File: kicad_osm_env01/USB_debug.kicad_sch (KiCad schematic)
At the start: 36 parts, among them J3 USB_B_Micro, Q2 S8050, Q3 S8050, U13 CP2102N-A01-GQFN24, U15 M74VHC1GT14DFT2G, U5 SP3003-02JTG

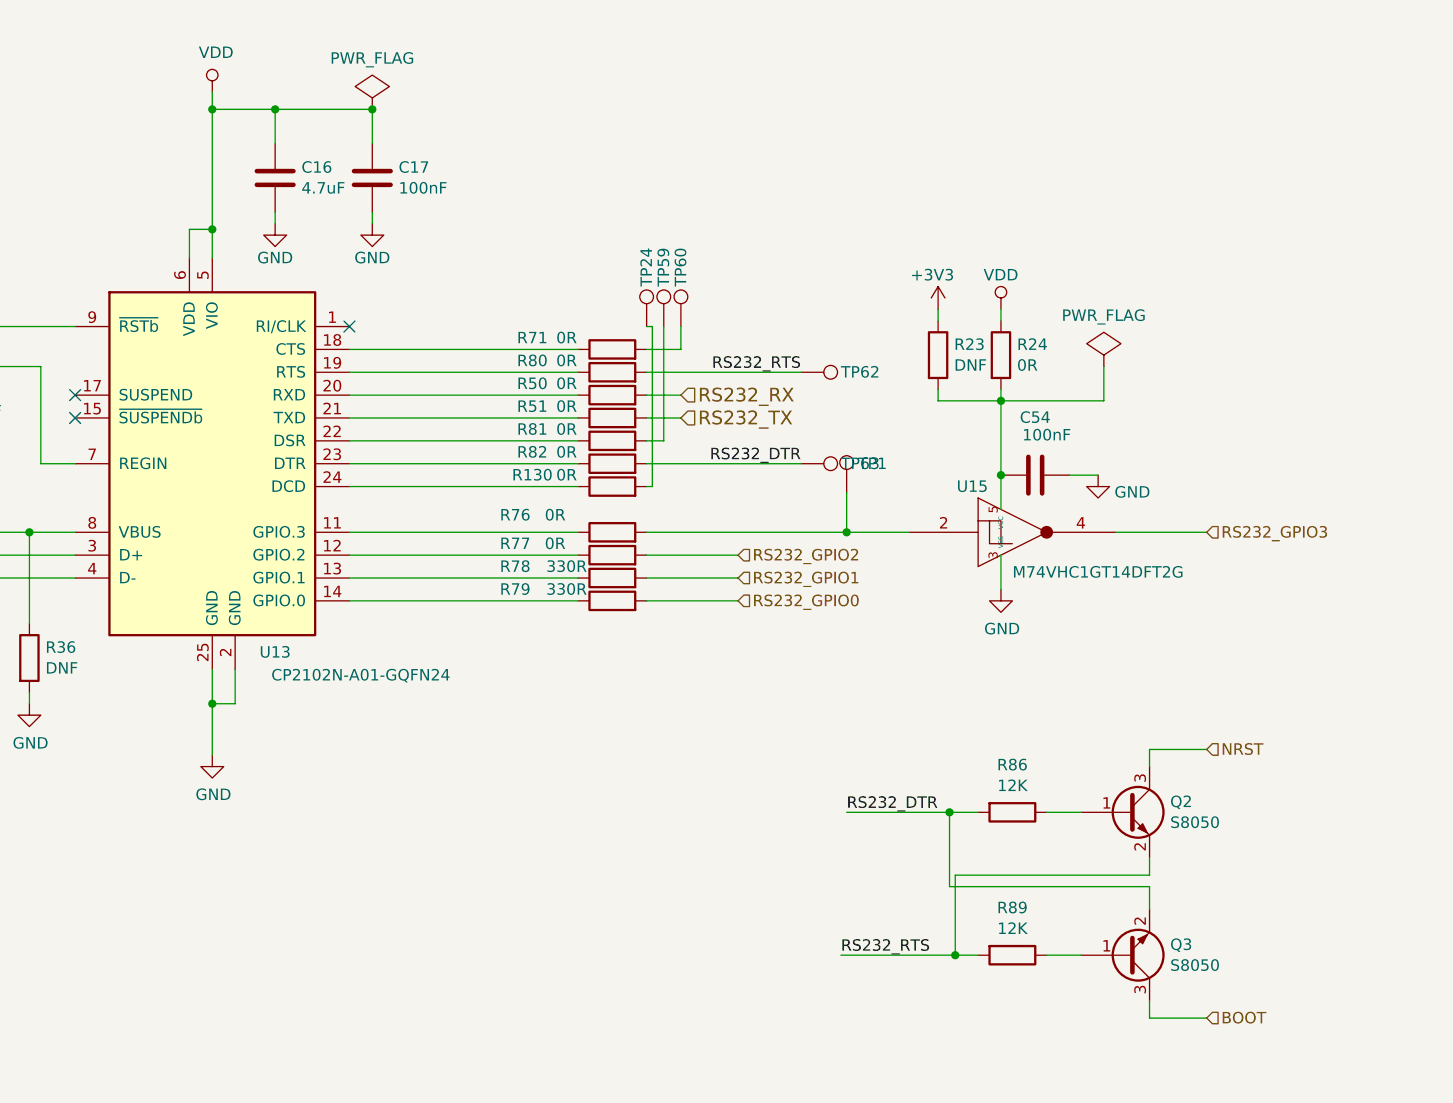
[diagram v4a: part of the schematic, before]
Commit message: Schematics waiting review
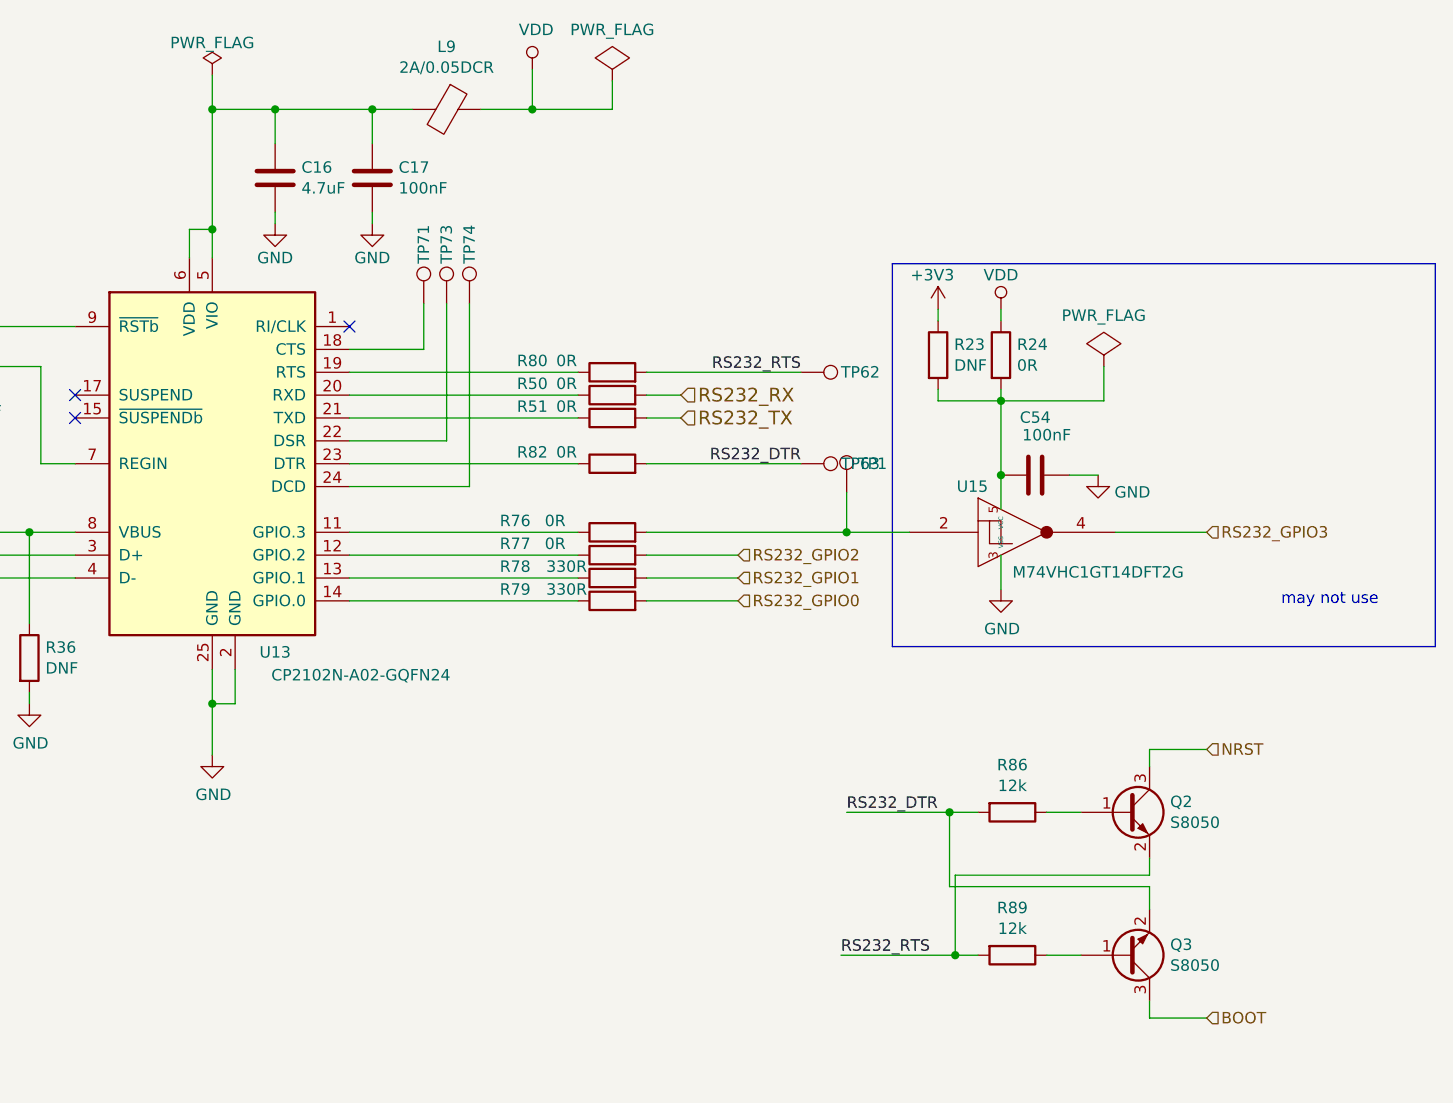
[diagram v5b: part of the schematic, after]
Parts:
- removed R130, R71, R81: 0R, Resistor_SMD:R_0603_1608Metric, symbol OSM_env01-rescue:R-device-ESP32-EVB_Rev_D-rescue
- removed TP24, TP59, TP60: Test_Point, TestPoint:TestPoint_Pad_D1.5mm, symbol Connector:Test_Point
- added L9: 2A/0.05DCR, Inductor_SMD:L_0402_1005Metric, symbol device:Ferrite_Bead
- added TP71, TP73, TP74: Test_Point, TestPoint:TestPoint_Pad_D1.5mm, symbol Connector:Test_Point
- R86, R89: value 12K -> 12k
- U13: value CP2102N-A01-GQFN24 -> CP2102N-A02-GQFN24
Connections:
- net VDD: now also L9.1; no longer C16.1, C17.1, U13.5 (VIO), U13.6 (VDD)
- net at U13.18 (CTS): now also TP71.1
- net at U13.22 (DSR): now also TP73.1
- net at U13.24 (DCD): now also TP74.1
- new net: C16.1, C17.1, L9.2, U13.5 (VIO), U13.6 (VDD)
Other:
- note added: "may not use"

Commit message: before fixing devtank symbol issues
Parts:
- added R152, R153: 0R, Resistor_SMD:R_0603_1608Metric, symbol device:R
- J3: value USB_B_Micro -> (none); footprint Devtank_PCB_lib:MOLEX_105017-0001_USB_B -> (none)
- TP1, TP63, TP71, TP73, TP74: value Test_Point -> (none); footprint TestPoint:TestPoint_Pad_D1.5mm -> (none); symbol Connector:Test_Point -> Connector:TestPoint
- TP62: footprint TestPoint:TestPoint_Pad_D1.5mm -> (none); symbol Connector:Test_Point -> Connector:TestPoint
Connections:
- net BOOT: now also R153.2; no longer Q3.3 (C)
- net NRST: now also R152.2; no longer Q2.3 (C)
- new net: Q2.3 (C), R152.1
- new net: Q3.3 (C), R153.1
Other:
- moved on the sheet: C54, R23, R24, TP1, U15

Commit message: started layout with throwdown
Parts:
- added R49: (no value), symbol Device:R
- added TP78: (no value), symbol Connector:TestPoint
- C15, C17, C54: value 100nF -> (none); footprint Capacitor_SMD:C_0402_1005Metric -> (none); symbol OSM_env01-rescue:C-device-ESP32-EVB_Rev_D-rescue -> Device:C
- C16: value 4.7uF -> (none); footprint Capacitor_SMD:C_0603_1608Metric -> (none); symbol OSM_env01-rescue:C-device-ESP32-EVB_Rev_D-rescue -> Device:C
- C47: value 4.7uF -> (none); footprint Capacitor_SMD:C_0603_1608Metric -> (none); symbol device:C -> Device:C
- C48: value 100nF -> (none); footprint Capacitor_SMD:C_0402_1005Metric -> (none); symbol device:C -> Device:C
- L9: value 2A/0.05DCR -> (none); footprint Inductor_SMD:L_0402_1005Metric -> (none); symbol device:Ferrite_Bead -> Device:FerriteBead
- Q2, Q3: value S8050 -> (none); footprint Package_TO_SOT_SMD:SOT-23 -> (none); symbol device:Q_NPN_BEC -> Device:Q_NPN_BEC
- R152, R153, R24, R35: value 0R -> (none); footprint Resistor_SMD:R_0603_1608Metric -> (none); symbol device:R -> Device:R
- R23, R36: value DNF -> (none); footprint Resistor_SMD:R_0603_1608Metric -> (none); symbol device:R -> Device:R
- R48: value 10k -> (none); footprint Resistor_SMD:R_0603_1608Metric -> (none); symbol OSM_env01-rescue:R-device-ESP32-EVB_Rev_D-rescue -> Device:R
- R50, R51, R76, R77, R80, R82: value 0R -> (none); footprint Resistor_SMD:R_0603_1608Metric -> (none); symbol OSM_env01-rescue:R-device-ESP32-EVB_Rev_D-rescue -> Device:R
- R78, R79: value 330R -> (none); footprint Resistor_SMD:R_0603_1608Metric -> (none); symbol OSM_env01-rescue:R-device-ESP32-EVB_Rev_D-rescue -> Device:R
- R86, R89: value 12k -> (none); footprint Resistor_SMD:R_0603_1608Metric -> (none); symbol device:R -> Device:R
- TP62: value Test_Point -> (none)
- U13: value CP2102N-A02-GQFN24 -> (none); footprint Devtank_PCB_lib:CP2102_QFN-24-1EP_4x4mm_P0.5mm_EP2.6x2.6mm_ThermalVias_0.3mmdrill -> (none)
- U15: value M74VHC1GT14DFT2G -> (none); footprint Package_TO_SOT_SMD:SOT-353_SC-70-5 -> (none)
- U5: value SP3003-02JTG -> (none); footprint Package_TO_SOT_SMD:SOT-353_SC-70-5 -> (none)
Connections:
- net BOOT is gone; now on an unnamed net: R153.2
- net at TP1.1, U15.2: no longer R76.2
- net RS232_DTR renamed USB_DEBUG_DTR
- net RS232_GPIO0 renamed USB_DEBUG_GPIO0
- net RS232_GPIO1 renamed USB_DEBUG_GPIO1
- net RS232_GPIO2 renamed USB_DEBUG_GPIO2
- net RS232_GPIO3: no longer names the net of U15.4
- net RS232_GPIO3: now also R49.1, TP78.1
- net RS232_RTS renamed USB_DEBUG_RTS
- net RS232_RX renamed USB_DEBUG_RX
- net RS232_TX renamed USB_DEBUG_TX
- new net BOOT0: R49.2
- new net USB_DEBUG_GPIO3: R76.2
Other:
- note removed: "may not use"
- moved on the sheet: C54, Q2, Q3, R152, R153, R23, R24, R86, R89, U15

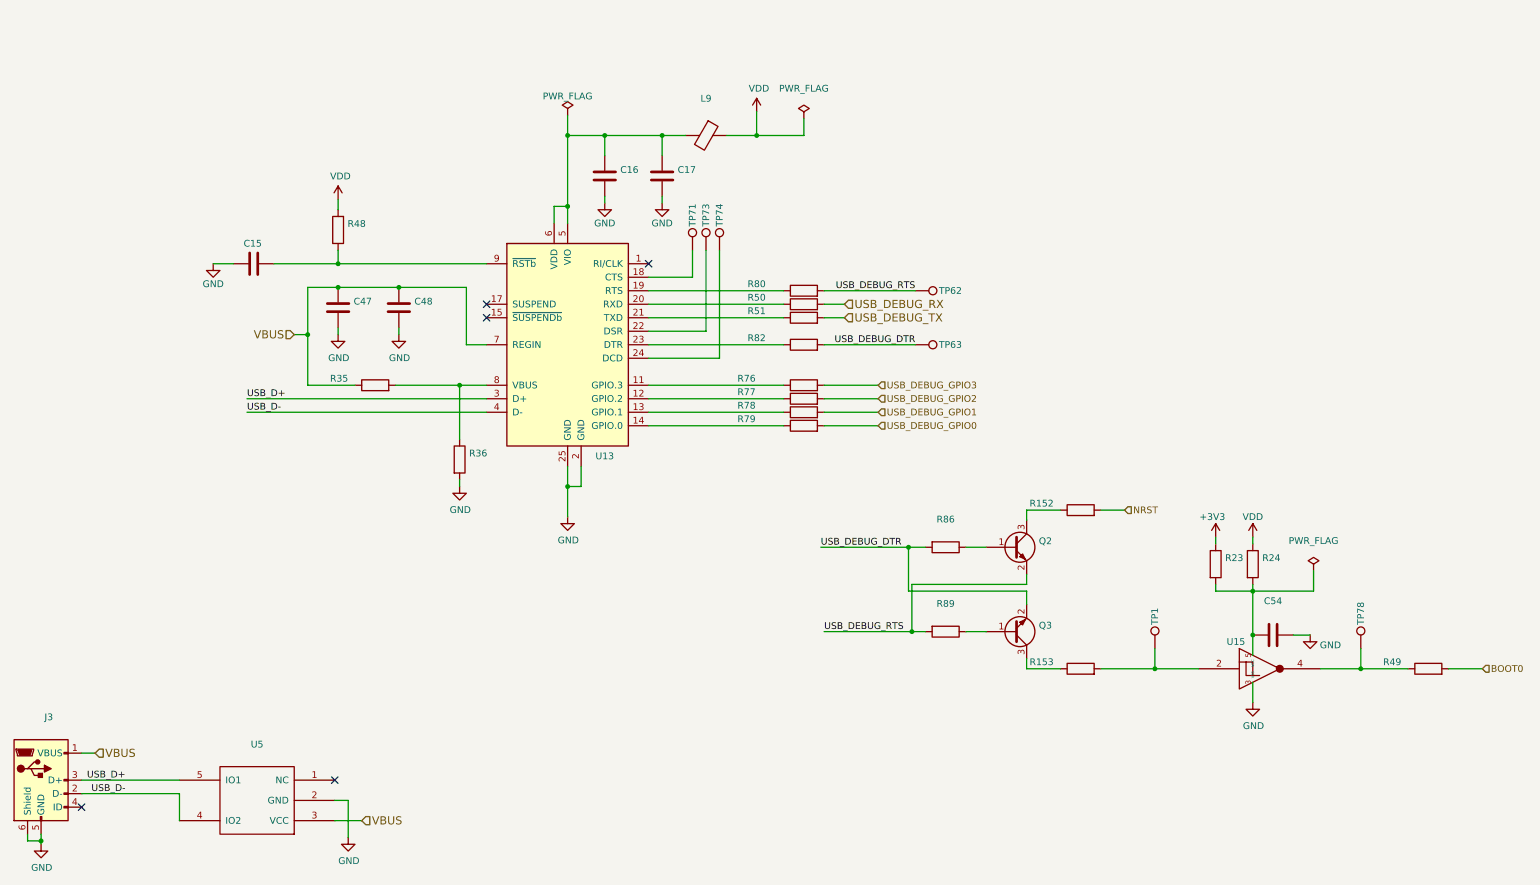
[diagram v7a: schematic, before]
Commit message: majority of signals routed on layout
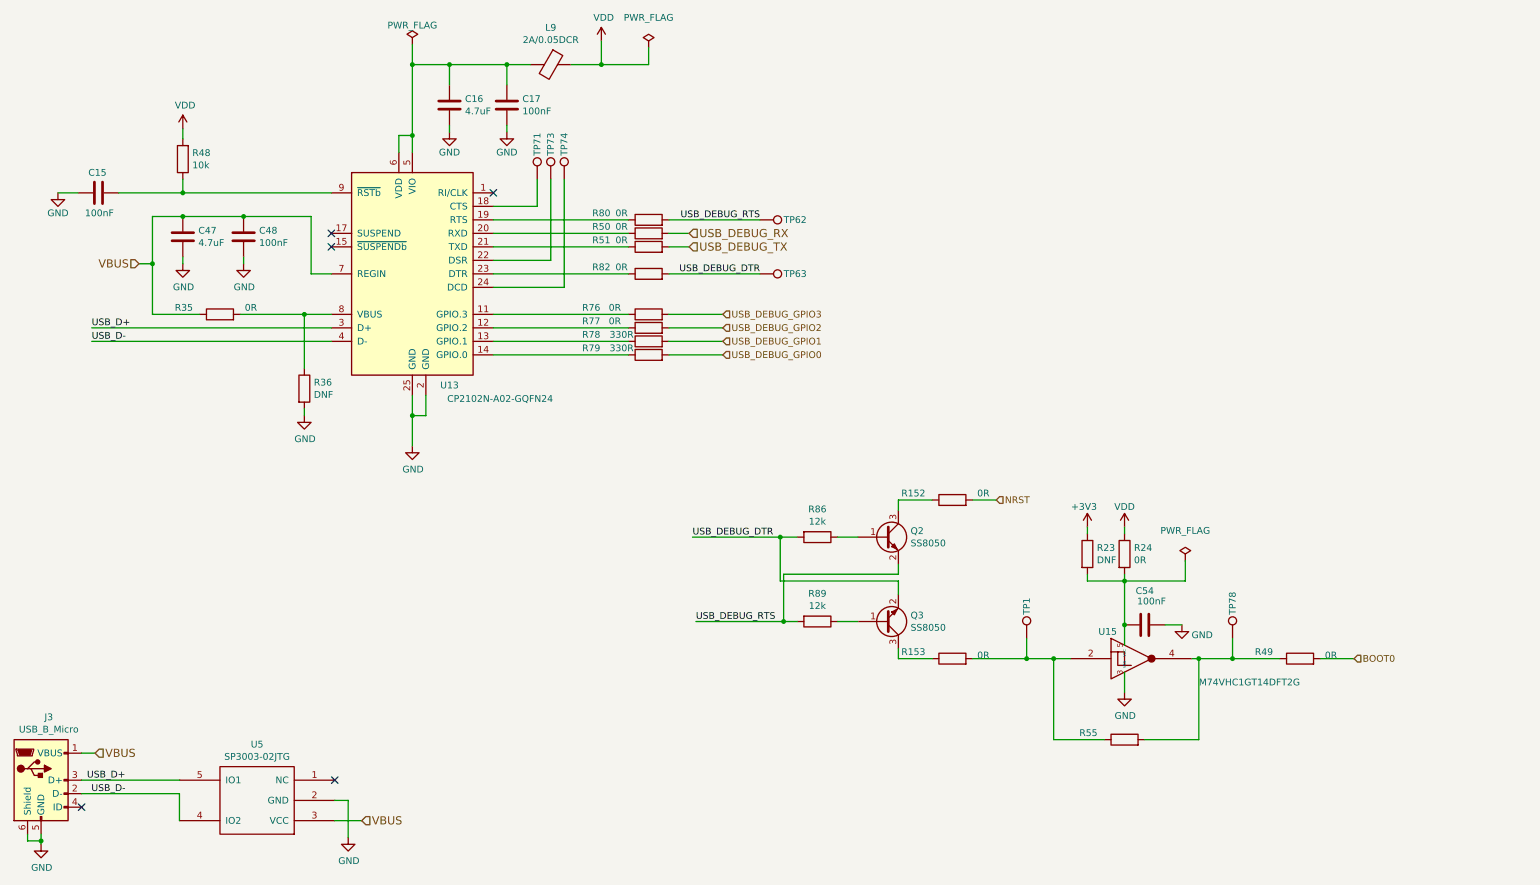
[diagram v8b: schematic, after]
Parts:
- added R55: (no value), symbol Device:R
- C15, C17, C48, C54: value (none) -> 100nF; footprint (none) -> Capacitor_SMD:C_0402_1005Metric
- C16, C47: value (none) -> 4.7uF; footprint (none) -> Capacitor_SMD:C_0402_1005Metric
- J3: value (none) -> USB_B_Micro; footprint (none) -> Devtank_PCB_lib:MOLEX_105017-0001_USB_B
- L9: value (none) -> 2A/0.05DCR; footprint (none) -> Inductor_SMD:L_0402_1005Metric
- Q2, Q3: value (none) -> SS8050; footprint (none) -> Package_TO_SOT_SMD:SOT-23
- R152, R153, R24, R35, R49, R50, R51, R76, R77, R80, R82: value (none) -> 0R; footprint (none) -> Resistor_SMD:R_0603_1608Metric
- R23, R36: value (none) -> DNF; footprint (none) -> Resistor_SMD:R_0603_1608Metric
- R48: value (none) -> 10k; footprint (none) -> Resistor_SMD:R_0603_1608Metric
- R78, R79: value (none) -> 330R; footprint (none) -> Resistor_SMD:R_0603_1608Metric
- R86, R89: value (none) -> 12k; footprint (none) -> Resistor_SMD:R_0603_1608Metric
- TP1, TP62, TP63, TP71, TP73, TP74, TP78: value (none) -> Test_Point; footprint (none) -> TestPoint:TestPoint_THTPad_D1.0mm_Drill0.5mm
- U13: value (none) -> CP2102N-A02-GQFN24; footprint (none) -> Devtank_PCB_lib:CP2102_QFN-24-1EP_4x4mm_P0.5mm_EP2.6x2.6mm_ThermalVias_0.3mmdrill
- U15: value (none) -> M74VHC1GT14DFT2G; footprint (none) -> Package_TO_SOT_SMD:SOT-353_SC-70-5
- U5: value (none) -> SP3003-02JTG; footprint (none) -> Package_TO_SOT_SMD:SOT-353_SC-70-5
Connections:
- net at R153.2, TP1.1, U15.2: now also R55.1
- net at R49.1, TP78.1, U15.4: now also R55.2
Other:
- moved on the sheet: C15, C16, C17, C47, C48, C54, L9, Q2, Q3, R152, R153, R23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
